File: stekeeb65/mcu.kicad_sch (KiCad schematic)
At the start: 14 parts

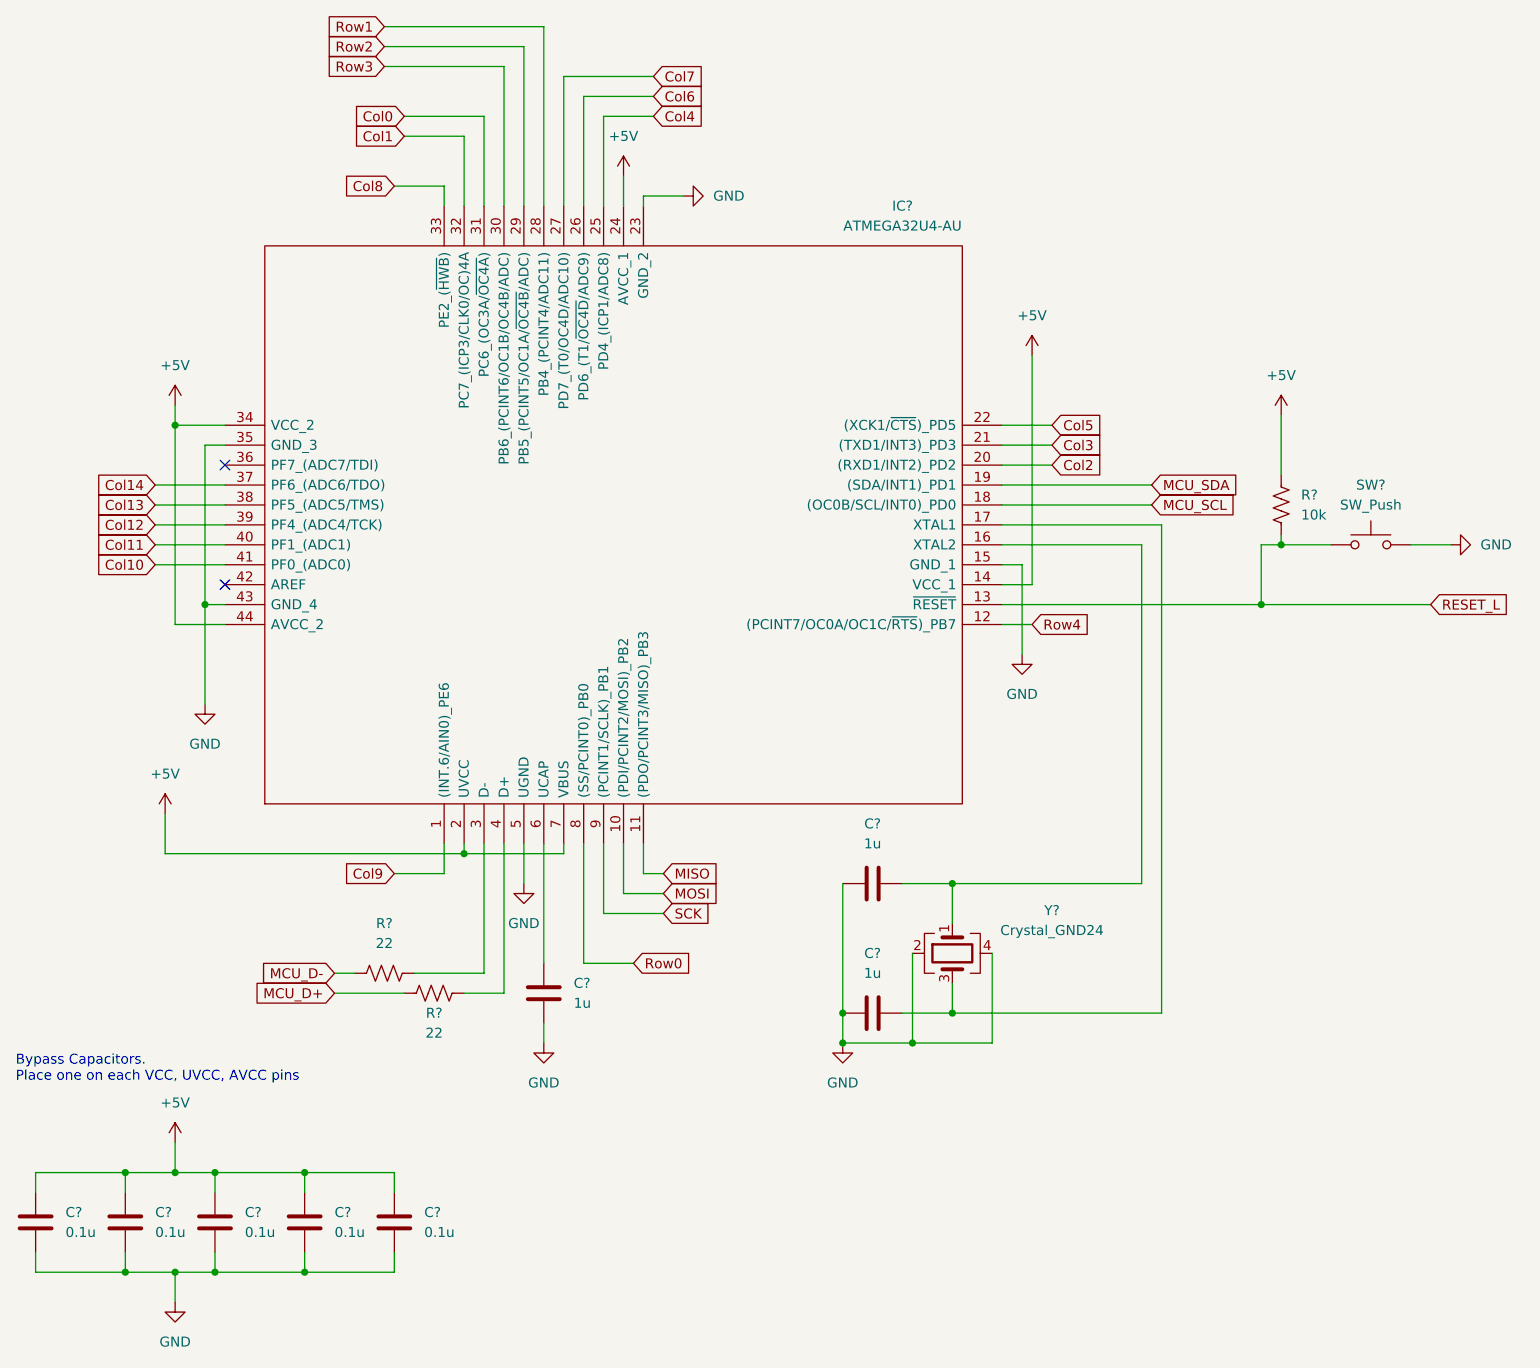
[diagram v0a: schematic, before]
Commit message: Adding keyboard footprints
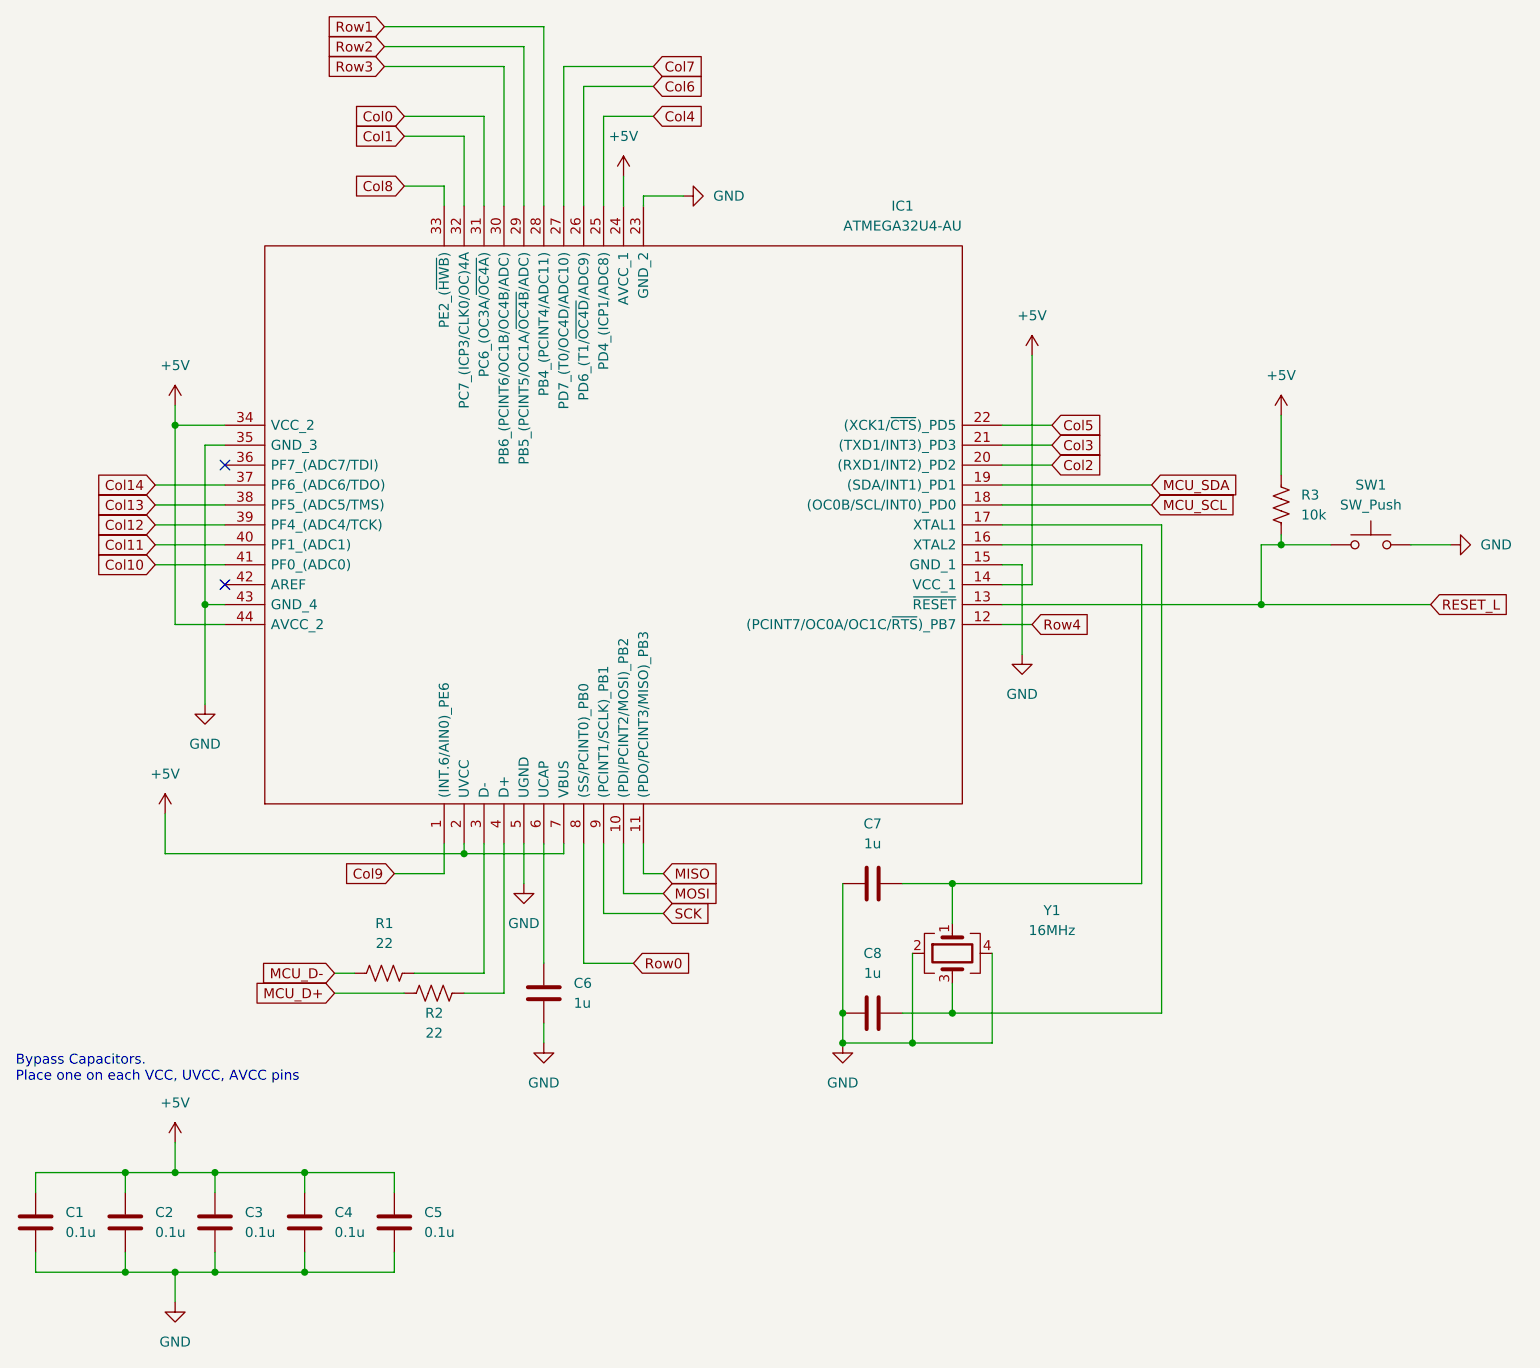
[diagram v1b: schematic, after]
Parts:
- C1, C2, C3, C4, C5, C6, C7, C8: renamed from C?; footprint (none) -> Capacitor_SMD:C_0805_2012Metric_Pad1.18x1.45mm_HandSolder
- R1, R2, R3: renamed from R?; footprint (none) -> Resistor_SMD:R_0805_2012Metric_Pad1.20x1.40mm_HandSolder
- Y1: renamed from Y?; value Crystal_GND24 -> 16MHz; footprint (none) -> Crystal:Crystal_SMD_3225-4Pin_3.2x2.5mm
- gave numbers to parts that had none: 2

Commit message: Committing before changes to PCB
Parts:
- SW1: footprint (none) -> random-keyboard-parts:RS187R05A2DSMTRT
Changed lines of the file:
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@@
     (property "Reference" "SW1" (id 0) (at 195.58 78.74 0))
     (property "Value" "SW_Push" (id 1) (at 195.58 81.28 0))
-    (property "Footprint" "" (id 2) (at 195.58 81.28 0)
+    (property "Footprint" "random-keyboard-parts:RS187R05A2DSMTRT" (id 2) (at 195.58 81.28 0)
       (effects (font (size 1.27 1.27)) hide)
     )
